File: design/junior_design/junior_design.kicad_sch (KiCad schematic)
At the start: 29 parts, among them J1 MPLAB SNAP, J2 Screw_Terminal_01x04, J3 Conn_01x05, J4 Conn_01x03, J5 USB_C_Receptacle_USB2.0_16P, U1 PIC24FJ64GA002-I_SP, U2 INA128, U3 TLV76133DCY, U4 MCP6022

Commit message: add pcb
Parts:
- C1: footprint (none) -> Capacitor_SMD:C_0805_2012Metric_Pad1.18x1.45mm_HandSolder
- C2, C3, C4, C5, C6, C7, C8, C9: footprint (none) -> Capacitor_SMD:C_0603_1608Metric_Pad1.08x0.95mm_HandSolder
- J1: footprint (none) -> Connector_PinHeader_2.54mm:PinHeader_1x08_P2.54mm_Horizontal
- J2: footprint (none) -> Connector_Phoenix_MC:PhoenixContact_MCV_1,5_4-G-3.81_1x04_P3.81mm_Vertical
- R1, R2, R3, R4, R5, R6, R7, R8, R9: footprint (none) -> Resistor_SMD:R_0603_1608Metric_Pad0.98x0.95mm_HandSolder
- U2, U4: footprint (none) -> Package_DIP:DIP-8_W7.62mm
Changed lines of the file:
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@@
 			)
 		)
-		(property "Footprint" ""
+		(property "Footprint" "Resistor_SMD:R_0603_1608Metric_Pad0.98x0.95mm_HandSolder"
 			(at 109.22 79.248 90)
 			(effects
@@
 			)
 		)
-		(property "Footprint" ""
+		(property "Footprint" "Resistor_SMD:R_0603_1608Metric_Pad0.98x0.95mm_HandSolder"
 			(at 74.422 53.34 90)
 			(effects
@@
 			)
 		)
-		(property "Footprint" ""
+		(property "Footprint" "Capacitor_SMD:C_0603_1608Metric_Pad1.08x0.95mm_HandSolder"
 			(at 229.5652 40.64 0)
 			(effects
@@
 			)
 		)
-		(property "Footprint" ""
+		(property "Footprint" "Capacitor_SMD:C_0603_1608Metric_Pad1.08x0.95mm_HandSolder"
 			(at 148.2852 45.72 0)
 			(effects
@@
 			)
 		)
-		(property "Footprint" ""
+		(property "Footprint" "Resistor_SMD:R_0603_1608Metric_Pad0.98x0.95mm_HandSolder"
 			(at 74.422 38.1 90)
 			(effects
@@
 			)
 		)
-		(property "Footprint" ""
+		(property "Footprint" "Resistor_SMD:R_0603_1608Metric_Pad0.98x0.95mm_HandSolder"
 			(at 61.722 53.34 90)
 			(effects
@@
 			)
 		)
-		(property "Footprint" ""
+		(property "Footprint" "Resistor_SMD:R_0603_1608Metric_Pad0.98x0.95mm_HandSolder"
 			(at 209.042 35.56 90)
 			(effects
@@
 			)
 		)
-		(property "Footprint" ""
+		(property "Footprint" "Package_DIP:DIP-8_W7.62mm"
 			(at 41.91 82.55 0)
 			(effects
@@
 			)
 		)
-		(property "Footprint" ""
+		(property "Footprint" "Capacitor_SMD:C_0603_1608Metric_Pad1.08x0.95mm_HandSolder"
 			(at 263.8552 73.66 0)
 			(effects
@@
 			)
 		)
-		(property "Footprint" ""
+		(property "Footprint" "Resistor_SMD:R_0603_1608Metric_Pad0.98x0.95mm_HandSolder"
 			(at 61.722 38.1 90)
 			(effects
@@
 			)
 		)
-		(property "Footprint" ""
+		(property "Footprint" "Connector_Phoenix_MC:PhoenixContact_MCV_1,5_4-G-3.81_1x04_P3.81mm_Vertical"
 			(at 24.13 146.05 0)
 			(effects
@@
 			)
 		)
-		(property "Footprint" ""
+		(property "Footprint" "Capacitor_SMD:C_0603_1608Metric_Pad1.08x0.95mm_HandSolder"
 			(at 249.8852 73.66 0)
 			(effects
@@
 			)
 		)
-		(property "Footprint" ""
+		(property "Footprint" "Capacitor_SMD:C_0603_1608Metric_Pad1.08x0.95mm_HandSolder"
 			(at 261.3152 40.64 0)
 			(effects
@@
 			)
 		)
-		(property "Footprint" ""
+		(property "Footprint" "Resistor_SMD:R_0603_1608Metric_Pad0.98x0.95mm_HandSolder"
 			(at 99.822 68.58 90)
 			(effects
@@
 			)
 		)
-		(property "Footprint" ""
+		(property "Footprint" "Resistor_SMD:R_0603_1608Metric_Pad0.98x0.95mm_HandSolder"
 			(at 217.932 35.56 90)
 			(effects
@@
 			)
 		)
-		(property "Footprint" ""
+		(property "Footprint" "Capacitor_SMD:C_0603_1608Metric_Pad1.08x0.95mm_HandSolder"
 			(at 20.0152 111.76 0)
 			(effects
@@
 			)
 		)
-		(property "Footprint" ""
+		(property "Footprint" "Connector_PinHeader_2.54mm:PinHeader_1x08_P2.54mm_Horizontal"
 			(at 234.95 116.84 0)
 			(effects
@@
 			)
 		)
-		(property "Footprint" ""
+		(property "Footprint" "Capacitor_SMD:C_0603_1608Metric_Pad1.08x0.95mm_HandSolder"
 			(at 21.2852 66.04 0)
 			(effects
@@
 			)
 		)
-		(property "Footprint" ""
+		(property "Footprint" "Package_DIP:DIP-8_W7.62mm"
 			(at 78.74 120.65 0)
 			(effects
@@
 			)
 		)
-		(property "Footprint" ""
+		(property "Footprint" "Resistor_SMD:R_0603_1608Metric_Pad0.98x0.95mm_HandSolder"
 			(at 23.622 82.55 90)
 			(effects
@@
 			)
 		)
-		(property "Footprint" ""
+		(property "Footprint" "Package_DIP:DIP-8_W7.62mm"
 			(at 34.29 107.95 0)
 			(effects
@@
 			)
 		)
-		(property "Footprint" ""
+		(property "Footprint" "Package_DIP:DIP-8_W7.62mm"
 			(at 78.74 95.25 0)
 			(effects
@@
 			)
 		)
-		(property "Footprint" ""
+		(property "Footprint" "Capacitor_SMD:C_0603_1608Metric_Pad1.08x0.95mm_HandSolder"
 			(at 54.3052 148.59 0)
 			(effects
@@
 			)
 		)
-		(property "Footprint" ""
+		(property "Footprint" "Capacitor_SMD:C_0805_2012Metric_Pad1.18x1.45mm_HandSolder"
 			(at 237.1852 86.36 0)
 			(effects

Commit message: Started PCB layout
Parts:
- added H1, H2, H3, H4: MountingHole, MountingHole:MountingHole_2.7mm, symbol Mechanical:MountingHole
- U100: renamed from U1; footprint PIC24FJ64GA002-I_SP:DIP787W46P254L3467H508Q28 -> Package_DIP:DIP-28_W7.62mm
- renumbered C1 to C100, C2 to C101, C3 to C102, C7 to C110, C6 to C111, C9 to C121, C8 to C130, C4 to C190, C5 to C191, J1 to J100, J2 to J111, J3 to J120, J4 to J121, J5 to J190, R7 to R100, R6 to R101, R1 to R110, R2 to R130, R4 to R131, R3 to R132, R5 to R133, R8 to R190, R9 to R191, RV2 to RV130, RV1 to RV131, U2 to U110, U4 to U130, U3 to U190
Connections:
- net GND: now also J190.S1 (SHIELD)
- net PWM0: now also U100.15 (PGC3/EMUC3/RP6/ASCL1/CN24/PMD6/RB6)
- net SCL0: now also U100.17 (TCK/RP8/SCL1/CN22/PMD4/RB8)
- net SDA0: now also U100.18 (TDO/RP9/SDA1/CN21/PMD3/RB9)

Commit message: Finish routing PCB
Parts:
- J111: footprint Connector_Phoenix_MC:PhoenixContact_MCV_1,5_4-G-3.81_1x04_P3.81mm_Vertical -> Connector_Phoenix_MC:PhoenixContact_MC_1,5_4-G-3.81_1x04_P3.81mm_Horizontal
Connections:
- net +3.3V: no longer C121.1
- net +5V: now also C121.1
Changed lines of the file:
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@@
+	)
+	(symbol
+		(lib_id "power:+5V")
+		(at 147.32 38.1 0)
+		(unit 1)
+		(exclude_from_sim no)
+		(in_bom yes)
+		(on_board yes)
+		(dnp no)
+		(fields_autoplaced yes)
+		(property "Reference" "#PWR0101"
+			(at 147.32 41.91 0)
+			(effects
+				(font
+					(size 1.27 1.27)
+				)
+				(hide yes)
+			)
+		)
+		(property "Value" "+5V"
+			(at 147.32 33.02 0)
+			(effects
+				(font
+					(size 1.27 1.27)
+				)
+			)
+		)
+		(property "Footprint" ""
+			(at 147.32 38.1 0)
+			(effects
+				(font
+					(size 1.27 1.27)
+				)
+				(hide yes)
+			)
+		)
+		(property "Datasheet" ""
+			(at 147.32 38.1 0)
+			(effects
+				(font
+					(size 1.27 1.27)
+				)
+				(hide yes)
+			)
+		)
+		(property "Description" "Power symbol creates a global label with name \"+5V\""
+			(at 147.32 38.1 0)
+			(effects
+				(font
+					(size 1.27 1.27)
+				)
+				(hide yes)
+			)
+		)
+		(pin "1"
+		)
+		(instances
+			(project "junior_design"
+				(path "/579d38b9-dfd2-4e74-84d9-ad5d94ed0bf7"
+					(reference "#PWR0101")
+					(unit 1)
+				)
+			)
+		)
 	)
 	(symbol
@@
 	)
 	(symbol
-		(lib_id "power:+3.3V")
-		(at 147.32 38.1 0)
-		(unit 1)
-		(exclude_from_sim no)
-		(in_bom yes)
-		(on_board yes)
-		(dnp no)
-		(fields_autoplaced yes)
-		(property "Reference" "#PWR038"
-			(at 147.32 41.91 0)
-			(effects
-				(font
-					(size 1.27 1.27)
-				)
-				(hide yes)
-			)
-		)
-		(property "Value" "+3.3V"
-			(at 147.32 33.02 0)
-			(effects
-				(font
-					(size 1.27 1.27)
-				)
-			)
-		)
-		(property "Footprint" ""
-			(at 147.32 38.1 0)
-			(effects
-				(font
-					(size 1.27 1.27)
-				)
-				(hide yes)
-			)
-		)
-		(property "Datasheet" ""
-			(at 147.32 38.1 0)
-			(effects
-				(font
-					(size 1.27 1.27)
-				)
-				(hide yes)
-			)
-		)
-		(property "Description" "Power symbol creates a global label with name \"+3.3V\""
-			(at 147.32 38.1 0)
-			(effects
-				(font
-					(size 1.27 1.27)
-				)
-				(hide yes)
-			)
-		)
-		(pin "1"
-		)
-		(instances
-			(project "junior_design"
-				(path "/579d38b9-dfd2-4e74-84d9-ad5d94ed0bf7"
-					(reference "#PWR038")
-					(unit 1)
-				)
-			)
-		)
-	)
-	(symbol
 		(lib_id "Device:R")
 		(at 63.5 53.34 0)
@@
 			)
 		)
-		(property "Footprint" "Connector_Phoenix_MC:PhoenixContact_MCV_1,5_4-G-3.81_1x04_P3.81mm_Vertical"
+		(property "Footprint" "Connector_Phoenix_MC:PhoenixContact_MC_1,5_4-G-3.81_1x04_P3.81mm_Horizontal"
 			(at 24.13 146.05 0)
 			(effects

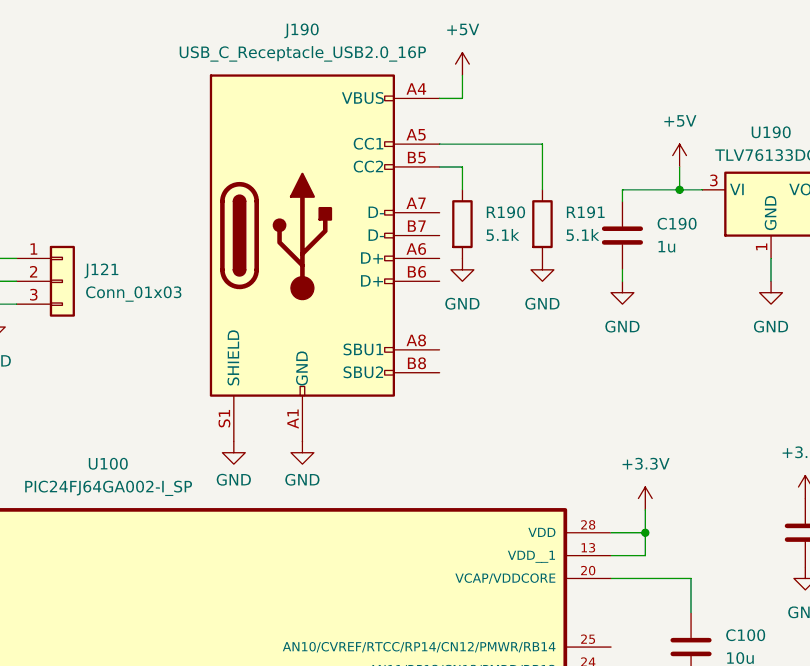
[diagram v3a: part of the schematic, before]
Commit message: add ferrite beads to usb-c port
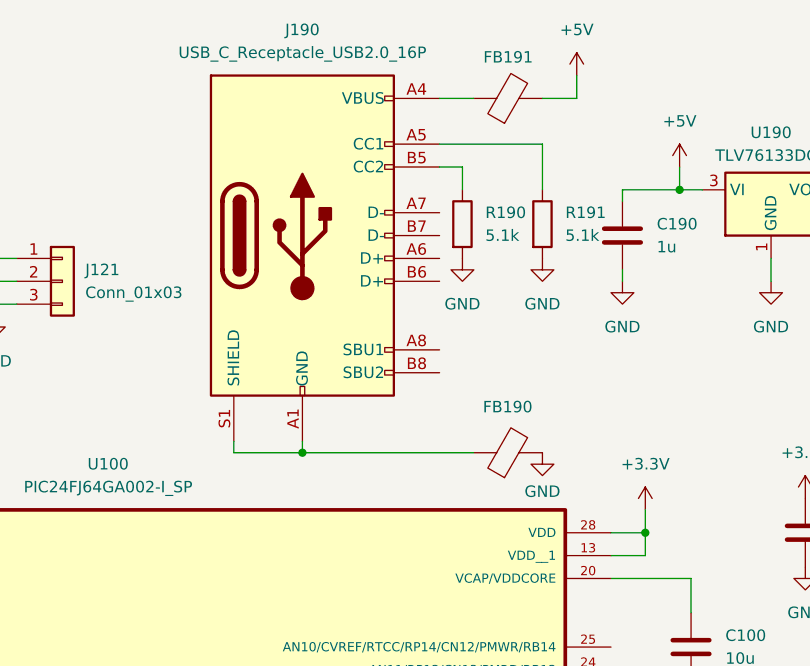
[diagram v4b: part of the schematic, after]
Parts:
- added FB190, FB191: FerriteBead, Inductor_SMD:L_0603_1608Metric_Pad1.05x0.95mm_HandSolder, symbol Device:FerriteBead
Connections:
- net +5V: now also FB191.2; no longer J190.A4 (VBUS), J190.A9 (VBUS), J190.B4 (VBUS), J190.B9 (VBUS)
- net GND: now also FB190.2; no longer J190.A1 (GND), J190.A12 (GND), J190.B1 (GND), J190.B12 (GND), J190.S1 (SHIELD)
- new net: FB190.1, J190.A1 (GND), J190.A12 (GND), J190.B1 (GND), J190.B12 (GND), J190.S1 (SHIELD)
- new net: FB191.1, J190.A4 (VBUS), J190.A9 (VBUS), J190.B4 (VBUS), J190.B9 (VBUS)
